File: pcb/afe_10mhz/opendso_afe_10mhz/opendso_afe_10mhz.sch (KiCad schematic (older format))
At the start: 12 parts, among them IC1 MCP47CVB02, J1 SAMTEC_HDBNC-J-P-GN-ST-TH1, J2 SAMTEC_HDBNC-J-P-GN-ST-TH1, J3 SAMTEC_LSS-140-01-L-DV-A

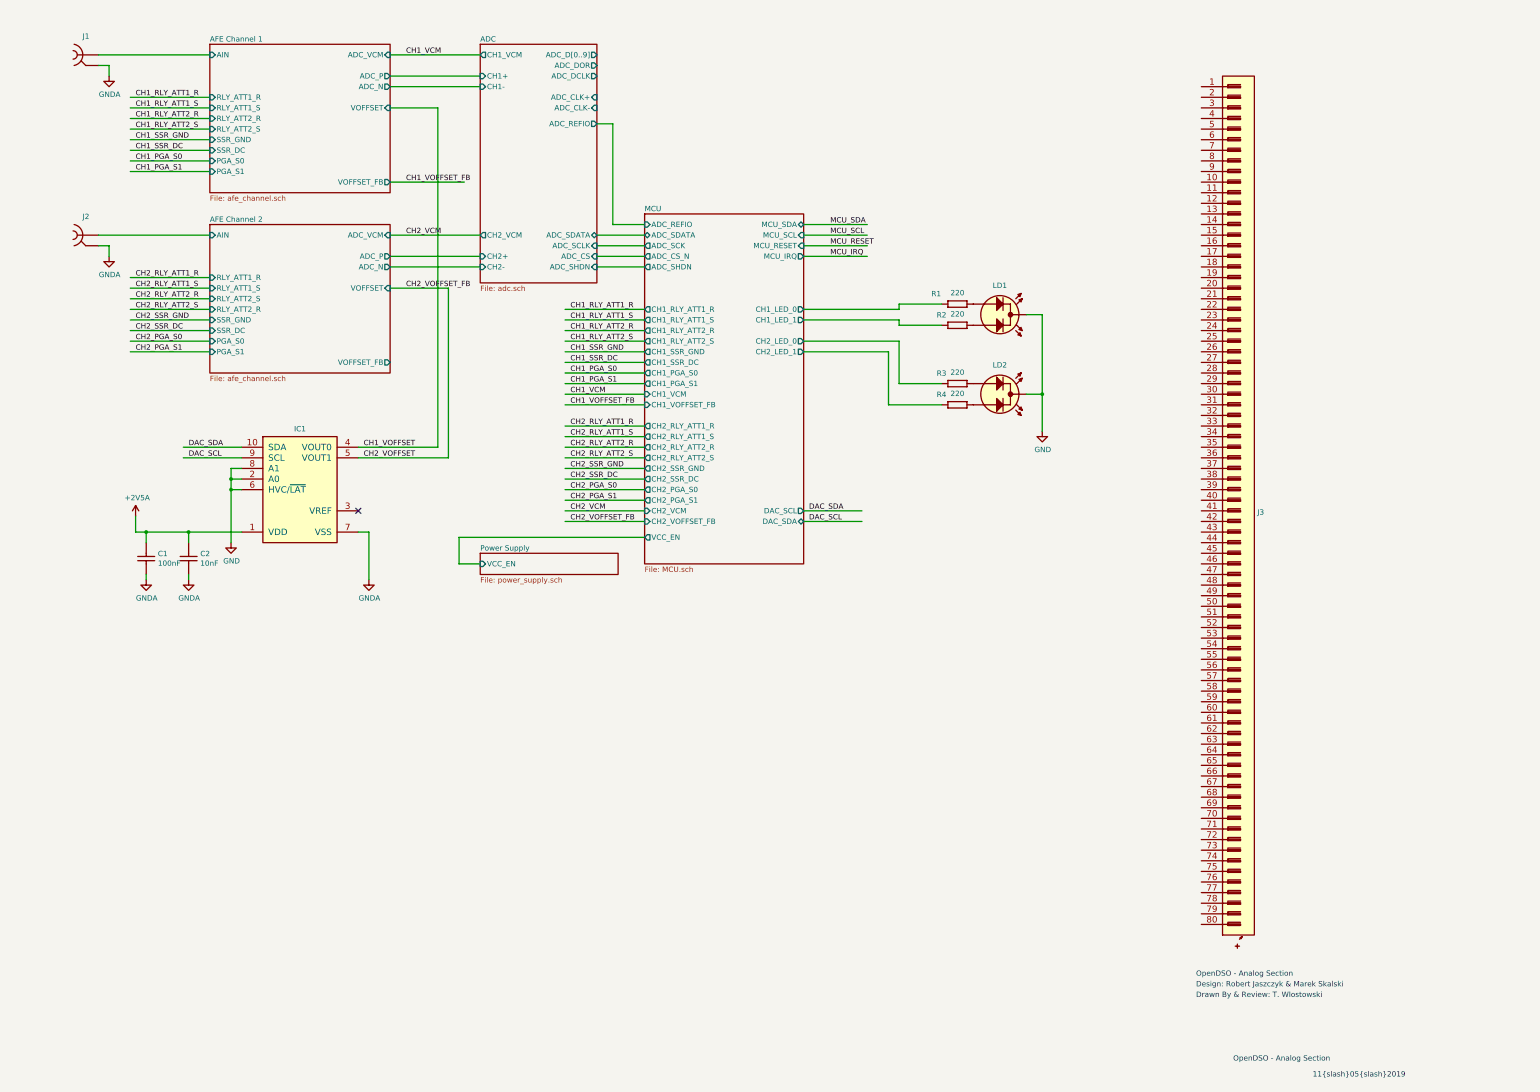
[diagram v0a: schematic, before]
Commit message: AFE schematic: finished port to KiCad
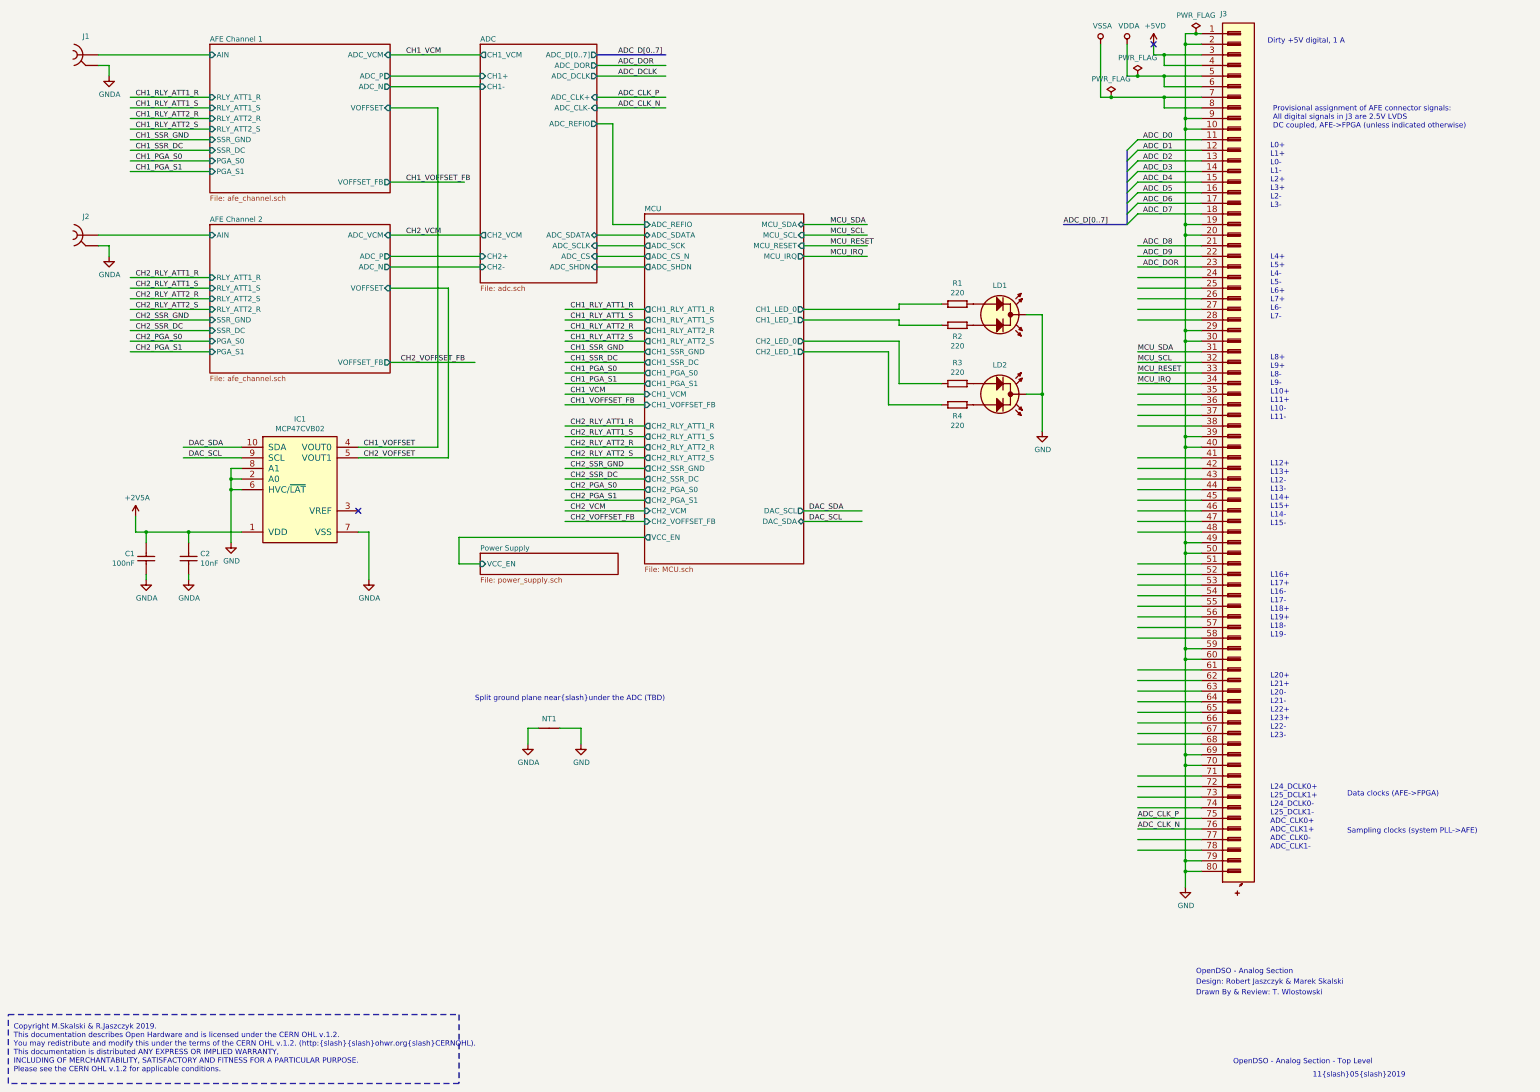
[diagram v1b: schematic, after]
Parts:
- added NT1: Net_Tie_2, Pads:Net Tie 2, symbol Pads:Net_Tie_2
- C1, C2: footprint CAPC1608X87N -> Capacitors SMD:CAPC1608X87N
- J1, J2: footprint SAMTEC THD:SAMTEC_HDBNC-J-P-GN-ST-TH1 -> Connector_Coaxial:BNC_TEConnectivity_1478204_Vertical
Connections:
- net labels added: +5VD, ADC_CLK_N, ADC_CLK_P, ADC_D0, ADC_D1, ADC_D2, ADC_D3, ADC_D4, ADC_D5, ADC_D6, ADC_D7, ADC_D8, ADC_D9, ADC_DCLK, ADC_DOR, ADC_D[0..7], VDDA, VSSA
- wire segments 105 -> 224
- no-connect marks 1 -> 2
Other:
- note added: "Copyright M.Skalski & R.Jaszczyk 2019.\nThis documentation describes Open Hardware and is licensed under the CERN OHL v.1.2.\nYou may redistribute and modify this under the terms of the CERN OHL v.1.2. (http://ohwr.org/CERNOHL).\nThis documentation is distributed ANY EXPRESS OR IMPLIED WARRANTY,\nINCLUDING OF MERCHANTABILITY, SATISFACTORY AND FITNESS FOR A PARTICULAR PURPOSE.\nP…"
- note added: "Data clocks (AFE->FPGA)"
- note added: "Dirty +5V digital, 1 A"
- note added: "L0+\nL1+\nL0-\nL1-\nL2+\nL3+\nL2-\nL3-"
- note added: "L12+\nL13+\nL12-\nL13-\nL14+\nL15+\nL14-\nL15-"
- note added: "L16+\nL17+\nL16-\nL17-\nL18+\nL19+\nL18-\nL19-"
- note added: "L20+\nL21+\nL20-\nL21-\nL22+\nL23+\nL22-\nL23-"
- note added: "L24_DCLK0+\nL25_DCLK1+\nL24_DCLK0-\nL25_DCLK1-\nADC_CLK0+\nADC_CLK1+\nADC_CLK0-\nADC_CLK1-"
- note added: "L4+\nL5+\nL4-\nL5-\nL6+\nL7+\nL6-\nL7-"
- note added: "L8+\nL9+\nL8-\nL9-\nL10+\nL11+\nL10-\nL11-"
- note added: "OpenDSO - Analog Section - Top Level\n"
- note added: "Provisional assignment of AFE connector signals:\nAll digital signals in J3 are 2.5V LVDS\nDC coupled, AFE->FPGA (unless indicated otherwise)"
- note added: "Sampling clocks (system PLL->AFE)"
- note added: "Split ground plane near/under the ADC (TBD)"
- moved on the sheet: J3

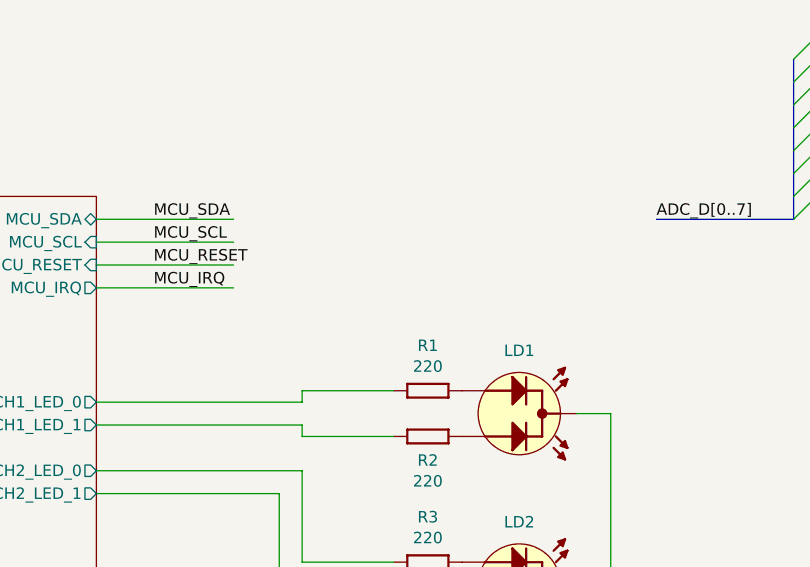
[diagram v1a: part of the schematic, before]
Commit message: pcb: added lcd_test_board design
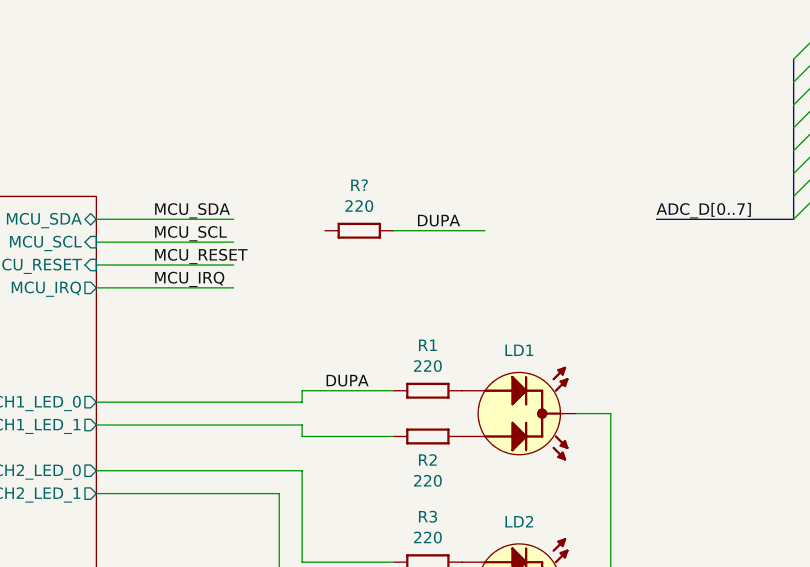
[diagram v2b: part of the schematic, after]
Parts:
- added R?: R0603_220R_1%_0.1W_100PPM, Resistors SMD:RESC1608X55N, symbol Resistors_SMD:R0603_220R_1%_0.1W_100PPM
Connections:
- net labels added: DUPA
- wire segments 224 -> 225
